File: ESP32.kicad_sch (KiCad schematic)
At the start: 18 parts, among them Q1 SS8050-G, Q2 SS8050-G, U2 ESP32-WROOM-32E-H4, U3 DF52-5S-0.8H(21), U5 CP2102N-A02-GQFN24R

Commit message: some placement and IMPORTANT schematic mistake fix from heirarchichal label importing
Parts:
- removed U3: DF52-5S-0.8H(21), robot-cortex:DF52-5S-0.8H(21), symbol robot-cortex:DF52-5S-0.8H(21)
- C1, C10, C11, C3: footprint robot-cortex:C_0603_1608Metric -> esp32-socket-switcher:C_0603_1608Metric; symbol robot-cortex:Capacitor -> esp32-socket-switcher:Capacitor
- C2, C4, C9: footprint robot-cortex:C_0402_1005Metric -> esp32-socket-switcher:C_0402_1005Metric; symbol robot-cortex:Capacitor -> esp32-socket-switcher:Capacitor
- Q1, Q2: footprint robot-cortex:SOT-23-3 -> esp32-socket-switcher:SOT-23-3; symbol robot-cortex:SS8050-G -> esp32-socket-switcher:SS8050-G
- R1, R2, R3, R4, R6, R9: footprint robot-cortex:R_0402_1005Metric -> esp32-socket-switcher:R_0402_1005Metric; symbol robot-cortex:Resistor -> esp32-socket-switcher:Resistor
- U2: footprint robot-cortex:ESP32-WROOM-32 -> esp32-socket-switcher:ESP32-WROOM-32; symbol robot-cortex:ESP32-WROOM-32E-H4 -> esp32-socket-switcher:ESP32-WROOM-32E-H4
- U5: footprint robot-cortex:QFN50P400X400X80-25N -> esp32-socket-switcher:QFN50P400X400X80-25N; symbol robot-cortex:CP2102N-A02-GQFN24R -> esp32-socket-switcher:CP2102N-A02-GQFN24R
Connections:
- net RELAY_OUT: now reaches U2.10 (IO25)
- net SWITCH_IN: now reaches U2.11 (IO26)

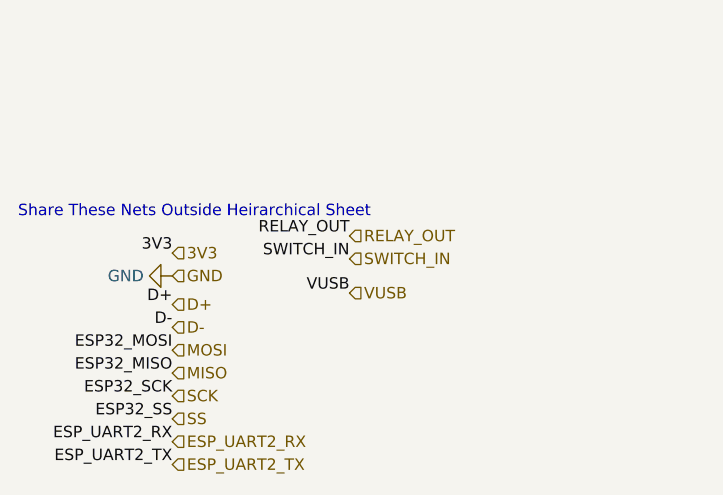
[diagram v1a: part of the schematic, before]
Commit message: added caps and placed them
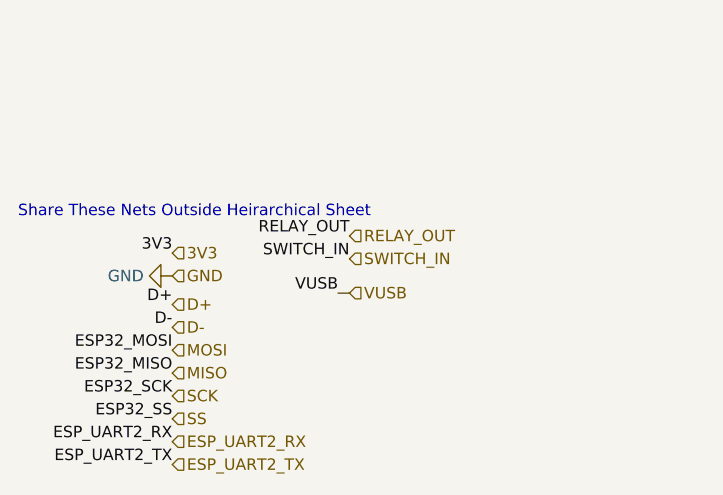
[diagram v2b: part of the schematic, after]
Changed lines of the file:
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@@
   (no_connect (at 211.455 128.905))
   (no_connect (at 257.175 139.065))
+  (wire (pts (xy 50.8 171.45) (xy 52.07 171.45))
+    (stroke (width 0) (type default))
+  )
   (wire (pts (xy 49.53 119.38) (xy 49.53 116.84))
     (stroke (width 0) (type default))
@@
     (effects (font (size 1.27 1.27)) (justify left bottom))
   )
-  (label "VUSB" (at 52.07 171.45 180) (fields_autoplaced)
-    (effects (font (size 1.27 1.27)) (justify right bottom))
-  )
+  (label "VUSB" (at 50.8 171.45 180) (fields_autoplaced)
+    (effects (font (size 1.27 1.27)) (justify right bottom))
+  )
